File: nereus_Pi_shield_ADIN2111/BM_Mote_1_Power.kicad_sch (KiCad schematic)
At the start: 26 parts, among them U10 LMR51430YDDCR, U5 LMR51430YDDCR, U6 TPS62840YBGR

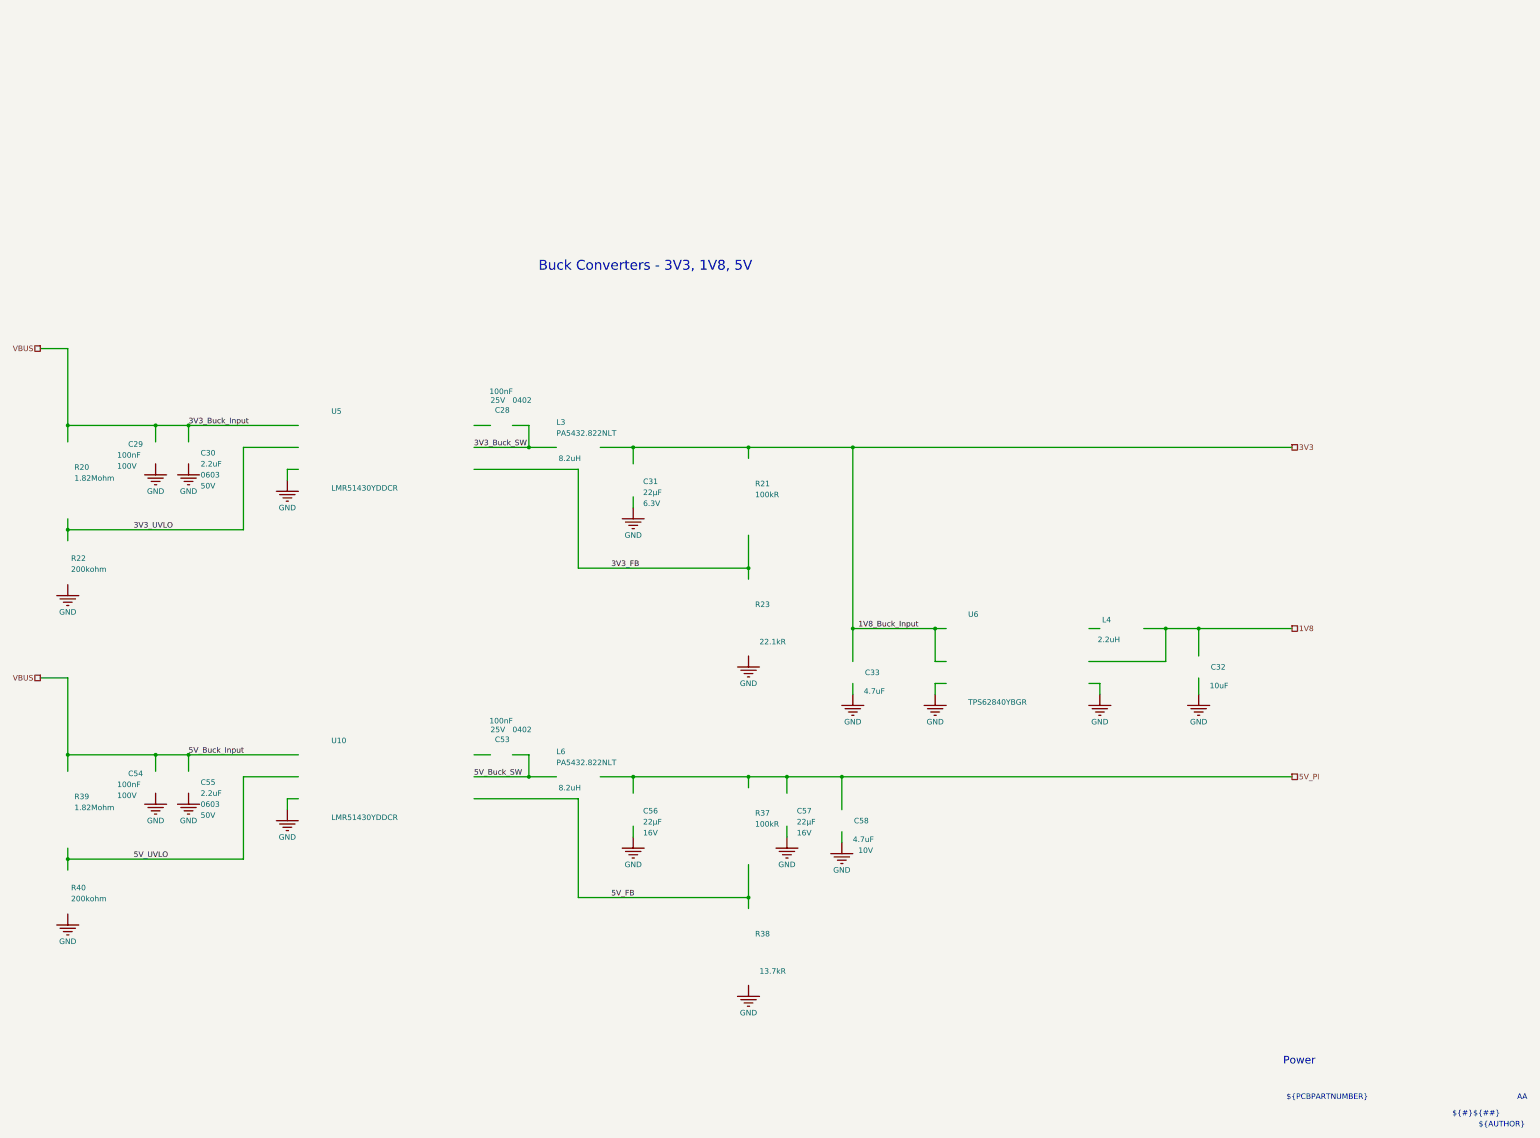
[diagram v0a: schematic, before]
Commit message: S6.g: presentation clean-up (Nick's list) + active-low names (D30)
- Top-Level: VBUS_OUT beside the Load Switch; I2C page-long runs ->
  labelled stubs at the PoDL pins; R43 beside the ADIN HW_EN pin; J5
  spaced with its note
- Cover: mote renders + old index -> grey TBD box + real sheet index;
  dimensions TBD; revision table inside the page, about this board;
  licence note and CC logo clear of the title block
- ADIN: supplies and LED blocks spaced from U1A, with headers
- Power: 3V3 / 1V8 / 5V converters spaced, with headers
- All sheets: KiCad title block filled; Altium overlay texts removed
- Names: ~{ADIN_RST}, ~{ADIN_INT}, ~{ADIN_CS}, ~{ADIN_P1/P2_LED1},
  PAYLOAD_EN, ~{PAYLOAD_FAULT} (labels, hier labels, sheet pins)
- Same pin partition; ERC 495 -> 492 / 0 errors; 8 exclusion keys
  regenerated (reasons unchanged); netcheck 51/51; midwire 0
- Docs: DESIGN D30 + pin map, changelog, README, sofar_brief, TRACKER,
  viewer, DEV_LOG; schematic.pdf re-exported

Co-Authored-By: Claude Opus 5.5 <noreply@anthropic.com>
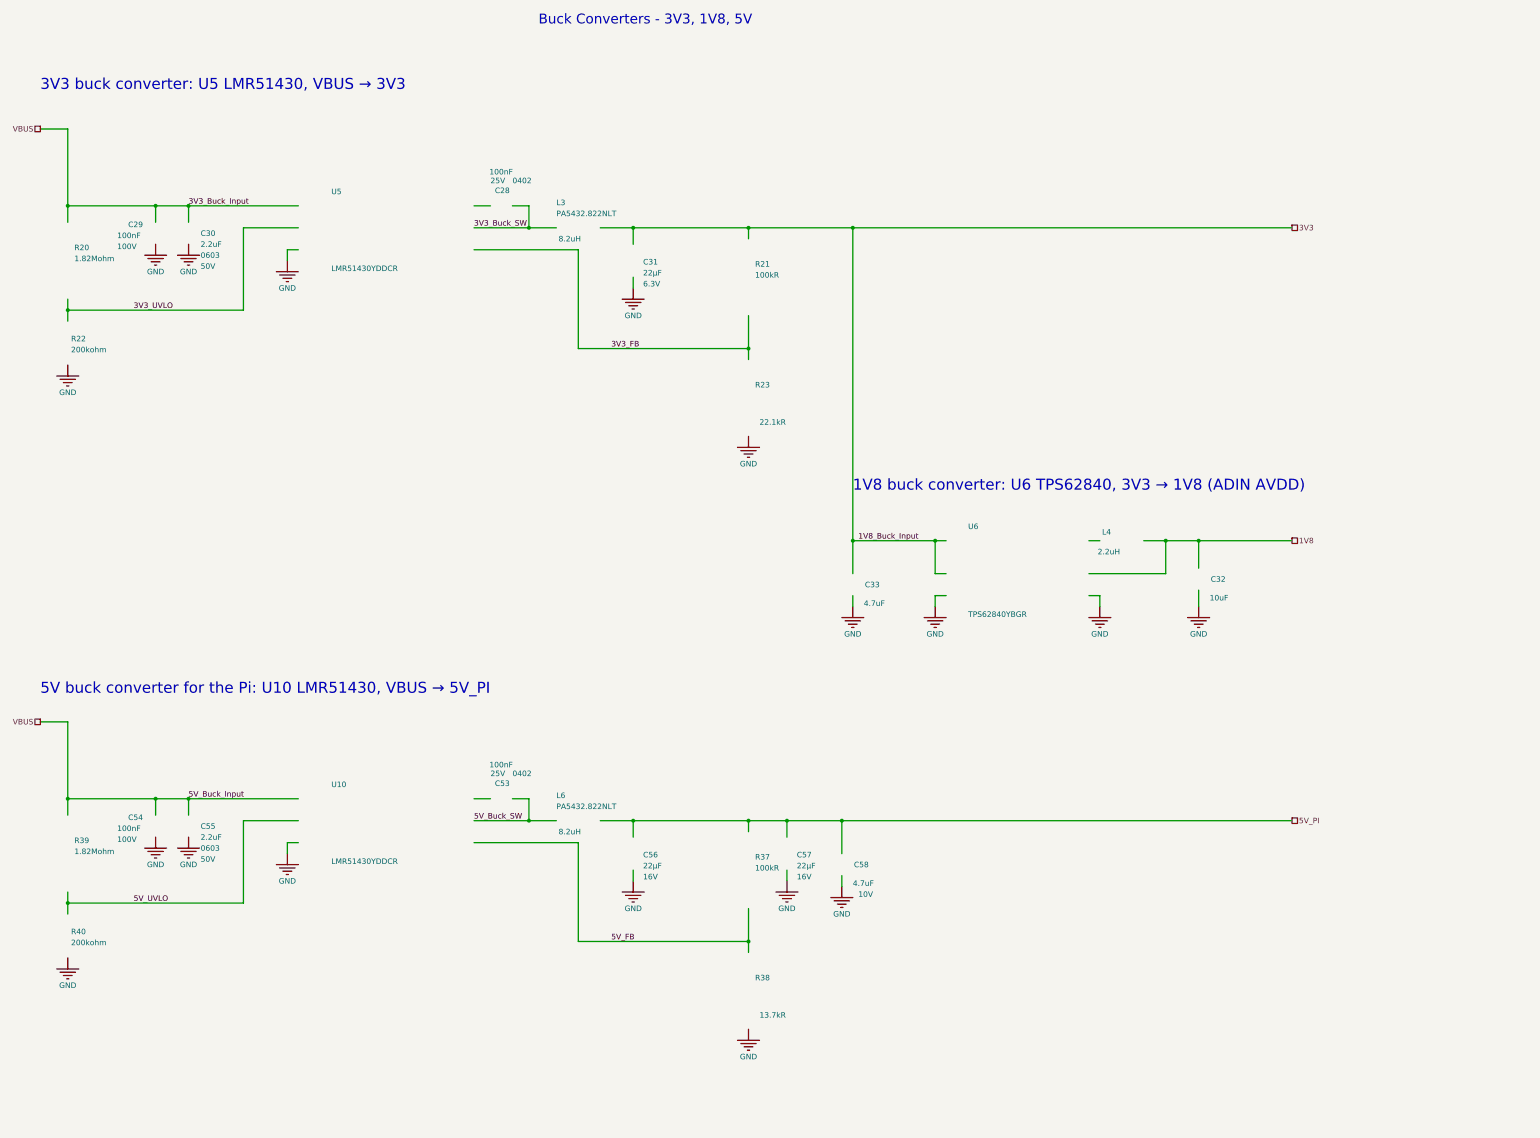
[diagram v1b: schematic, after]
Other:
- note added: "1V8 buck converter: U6 TPS62840, 3V3 → 1V8 (ADIN AVDD)"
- note added: "3V3 buck converter: U5 LMR51430, VBUS → 3V3"
- note added: "5V buck converter for the Pi: U10 LMR51430, VBUS → 5V_PI"
- note removed: "${##}"
- note removed: "${#}"
- note removed: "${AUTHOR}"
- note removed: "${PCBPARTNUMBER}"
- note removed: "${REVISION}"
- note removed: "${TITLE}"
